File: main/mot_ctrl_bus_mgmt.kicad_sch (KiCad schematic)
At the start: 20 parts, among them Q1101 IRLML0030, U1101 74LS08

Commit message: Clean silkscreen
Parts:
- renumbered C1101 to C1601, D1101 to D1601, D1102 to D1602, D1103 to D1603, D1104 to D1604, D1105 to D1605, D1106 to D1606, JP1101 to JP1601, JP1102 to JP1602, JP1103 to JP1603, JP1104 to JP1604, Q1101 to Q1601, R1101 to R1601, R1102 to R1602, R1103 to R1603, R1104 to R1604, R1105 to R1605, R1106 to R1606, R1107 to R1607, U1101 to U1601

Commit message: Sent to fab
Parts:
- C1601: MPN (none) -> CL21B104KACNFNC; Mouser SKU (none) -> 187-CL21B104KACNFNC
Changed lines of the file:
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@@
+			)
+		)
+		(property "Quantity" ""
+			(at 231.14 48.26 0)
+			(effects
+				(font
+					(size 1.27 1.27)
+				)
 			)
 		)
@@
 			)
 		)
+		(property "Quantity" ""
+			(at 208.28 57.15 0)
+			(effects
+				(font
+					(size 1.27 1.27)
+				)
+			)
+		)
 		(pin "1"
 		)
@@
 			)
 		)
+		(property "Quantity" ""
+			(at 208.28 48.26 0)
+			(effects
+				(font
+					(size 1.27 1.27)
+				)
+			)
+		)
 		(pin "1"
 		)
@@
 			)
 		)
+		(property "Quantity" ""
+			(at 255.27 57.15 0)
+			(effects
+				(font
+					(size 1.27 1.27)
+				)
+			)
+		)
 		(pin "1"
 		)
@@
 				)
 				(hide yes)
+			)
+		)
+		(property "Quantity" ""
+			(at 219.71 57.15 0)
+			(effects
+				(font
+					(size 1.27 1.27)
+				)
 			)
 		)
@@
 			)
 		)
+		(property "Quantity" ""
+			(at 99.06 151.13 0)
+			(effects
+				(font
+					(size 1.27 1.27)
+				)
+			)
+		)
 		(pin "6"
 		)
@@
 			)
 		)
+		(property "Quantity" ""
+			(at 99.06 45.72 0)
+			(effects
+				(font
+					(size 1.27 1.27)
+				)
+			)
+		)
 		(pin "6"
 		)
@@
 			)
 		)
+		(property "Quantity" ""
+			(at 266.7 48.26 0)
+			(effects
+				(font
+					(size 1.27 1.27)
+				)
+			)
+		)
 		(pin "1"
 		)
@@
 			)
 		)
+		(property "MPN" "CL21B104KACNFNC "
+			(at 109.22 45.72 0)
+			(effects
+				(font
+					(size 1.27 1.27)
+				)
+			)
+		)
+		(property "Mouser SKU" " 187-CL21B104KACNFNC "
+			(at 109.22 45.72 0)
+			(effects
+				(font
+					(size 1.27 1.27)
+				)
+			)
+		)
+		(property "Quantity" ""
+			(at 109.22 45.72 0)
+			(effects
+				(font
+					(size 1.27 1.27)
+				)
+			)
+		)
 		(pin "1"
 		)
@@
 			)
 		)
+		(property "Quantity" ""
+			(at 99.06 100.33 0)
+			(effects
+				(font
+					(size 1.27 1.27)
+				)
+			)
+		)
 		(pin "6"
 		)
@@
 			)
 		)
+		(property "Quantity" ""
+			(at 109.22 93.98 0)
+			(effects
+				(font
+					(size 1.27 1.27)
+				)
+			)
+		)
 		(pin "2"
 		)
@@
 			)
 		)
+		(property "Quantity" ""
+			(at 250.19 81.28 0)
+			(effects
+				(font
+					(size 1.27 1.27)
+				)
+			)
+		)
 		(pin "2"
 		)
@@
 			)
 		)
+		(property "Quantity" ""
+			(at 243.84 57.15 0)
+			(effects
+				(font
+					(size 1.27 1.27)
+				)
+			)
+		)
 		(pin "1"
 		)
@@
 			)
 		)
+		(property "Quantity" ""
+			(at 109.22 119.38 0)
+			(effects
+				(font
+					(size 1.27 1.27)
+				)
+			)
+		)
 		(pin "2"
 		)
@@
 			)
 		)
+		(property "Quantity" ""
+			(at 109.22 144.78 0)
+			(effects
+				(font
+					(size 1.27 1.27)
+				)
+			)
+		)
 		(pin "2"
 		)
@@
 			)
 		)
+		(property "Quantity" ""
+			(at 99.06 26.67 0)
+			(effects
+				(font
+					(size 1.27 1.27)
+				)
+			)
+		)
 		(pin "2"
 		)
@@
 			)
 		)
+		(property "Quantity" ""
+			(at 231.14 57.15 0)
+			(effects
+				(font
+					(size 1.27 1.27)
+				)
+			)
+		)
 		(pin "1"
 		)
@@
 			)
 		)
+		(property "Quantity" ""
+			(at 266.7 57.15 0)
+			(effects
+				(font
+					(size 1.27 1.27)
+				)
+			)
+		)
 		(pin "1"
 		)
@@
 			)
 		)
+		(property "Quantity" ""
+			(at 99.06 171.45 0)
+			(effects
+				(font
+					(size 1.27 1.27)
+				)
+			)
+		)
 		(pin "6"
 		)
@@
 			)
 		)
+		(property "Quantity" ""
+			(at 255.27 48.26 0)
+			(effects
+				(font
+					(size 1.27 1.27)
+				)
+			)
+		)
 		(pin "1"
 		)
@@
 				)
 				(hide yes)
+			)
+		)
+		(property "Quantity" ""
+			(at 264.16 76.2 0)
+			(effects
+				(font
+					(size 1.27 1.27)
+				)
 			)
 		)
@@
 			)
 		)
+		(property "Quantity" ""
+			(at 99.06 125.73 0)
+			(effects
+				(font
+					(size 1.27 1.27)
+				)
+			)
+		)
 		(pin "6"
 		)
@@
 			)
 		)
+		(property "Quantity" ""
+			(at 243.84 48.26 0)
+			(effects
+				(font
+					(size 1.27 1.27)
+				)
+			)
+		)
 		(pin "1"
 		)
@@
 			)
 		)
+		(property "Quantity" ""
+			(at 219.71 48.26 0)
+			(effects
+				(font
+					(size 1.27 1.27)
+				)
+			)
+		)

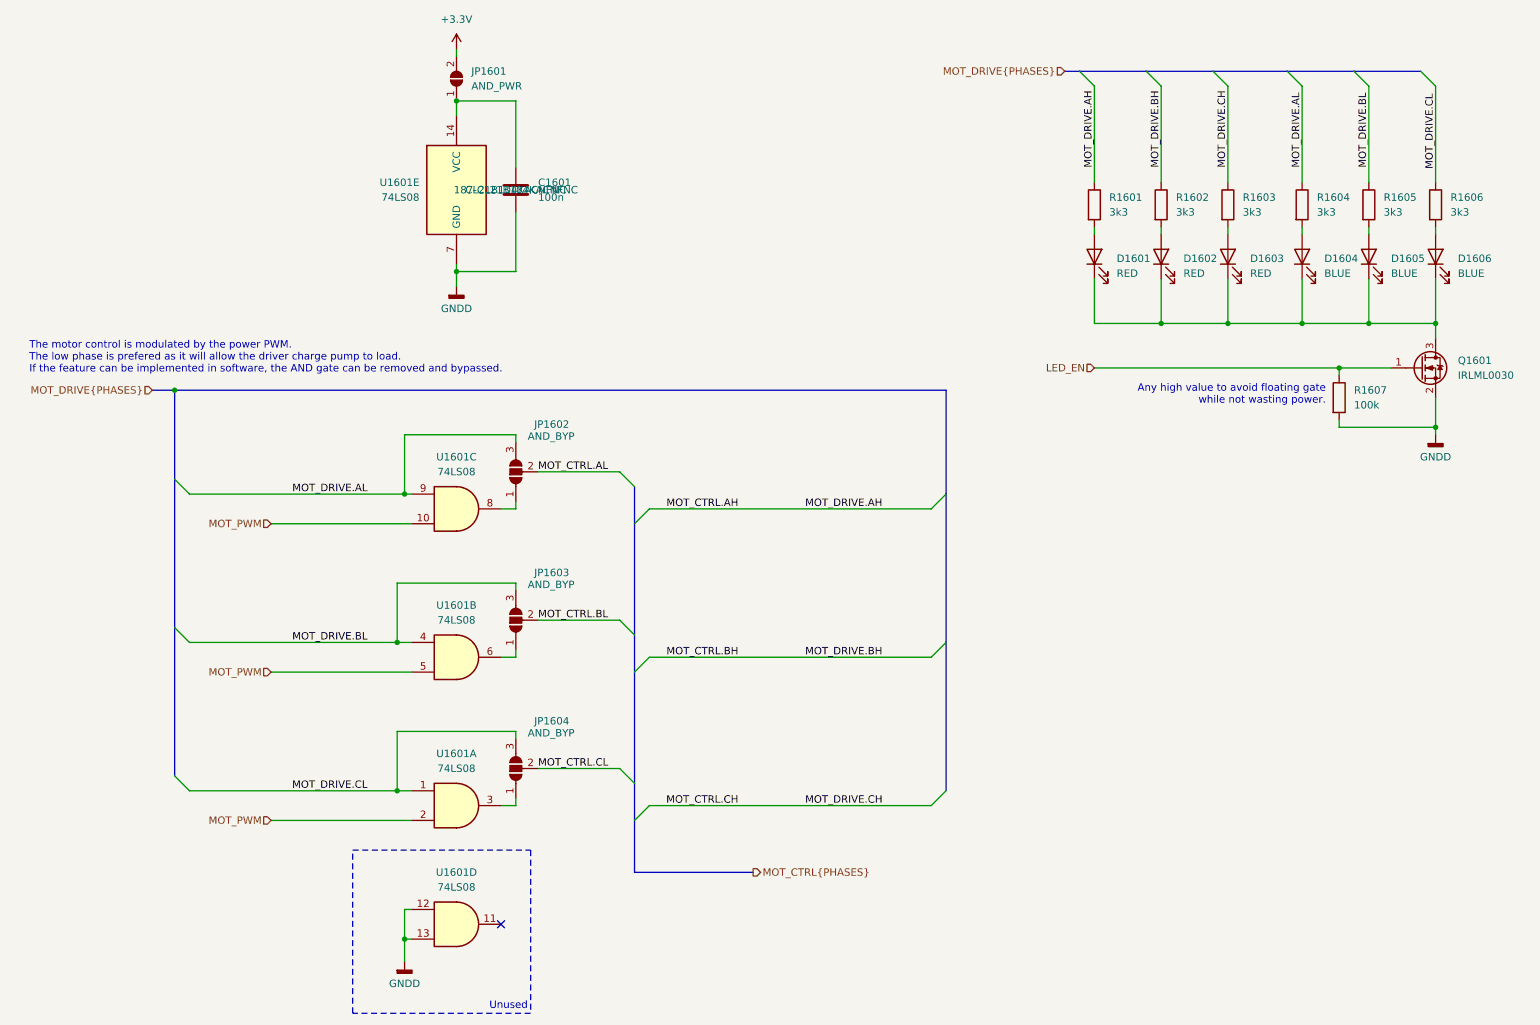
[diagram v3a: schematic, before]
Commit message: BOM almost OK, starts new side board.
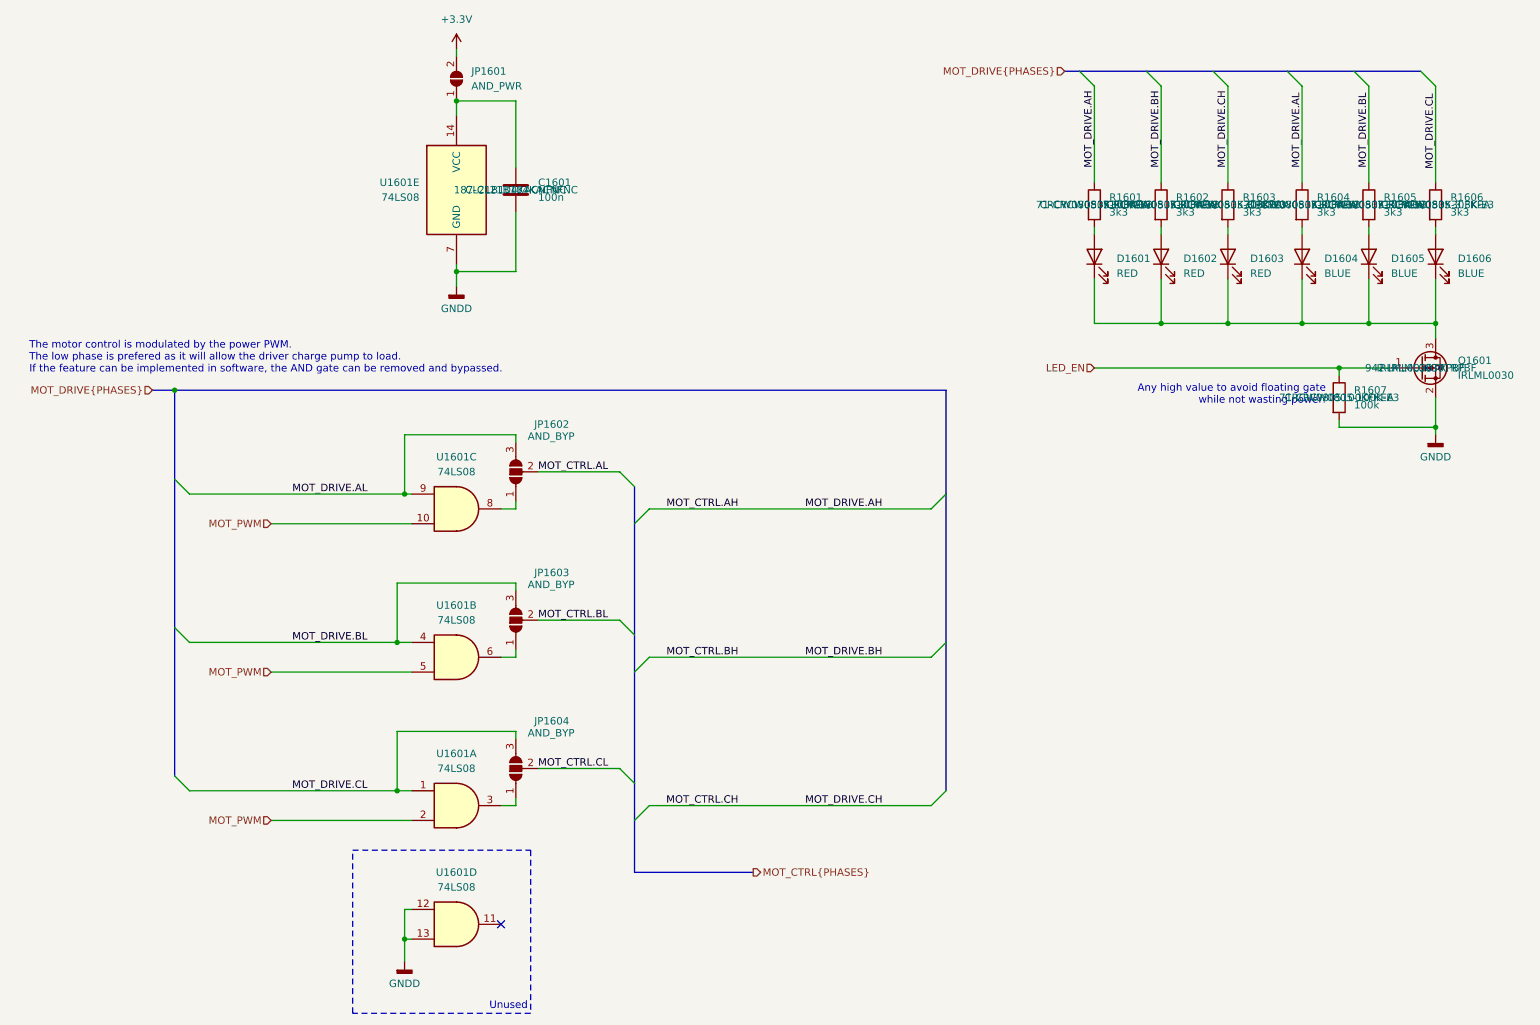
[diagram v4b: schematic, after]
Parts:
- JP1601, JP1602, JP1603, JP1604: now left out of the parts list
- Q1601: MPN (none) -> IRLML0030TRPBF; Mouser SKU (none) -> 942-IRLML0030TRPBF
- R1601, R1602, R1603, R1604, R1605, R1606: MPN (none) -> CRCW08053K30FKEA; Mouser SKU (none) -> 71-CRCW0805-3.3K-E3
- R1607: MPN (none) -> CRCW0805100KFKEA; Mouser SKU (none) -> 71-CRCW0805-100K-E3
- U1601: MPN 74LVC08ABQ,115 -> (none)
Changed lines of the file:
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@@
 (kicad_sch
-	(version 20240101)
+	(version 20240417)
 	(generator "eeschema")
 	(generator_version "8.99")
@@
 			)
 		)
+		(property "MPN" "CRCW08053K30FKEA"
+			(at 231.14 48.26 0)
+			(effects
+				(font
+					(size 1.27 1.27)
+				)
+			)
+		)
+		(property "Mouser SKU" " 71-CRCW0805-3.3K-E3 "
+			(at 231.14 48.26 0)
+			(effects
+				(font
+					(size 1.27 1.27)
+				)
+			)
+		)
 		(pin "1"
 		)
@@
 			)
 		)
+		(property "MPN" "CRCW08053K30FKEA"
+			(at 208.28 48.26 0)
+			(effects
+				(font
+					(size 1.27 1.27)
+				)
+			)
+		)
+		(property "Mouser SKU" " 71-CRCW0805-3.3K-E3 "
+			(at 208.28 48.26 0)
+			(effects
+				(font
+					(size 1.27 1.27)
+				)
+			)
+		)
 		(pin "1"
 		)
@@
 			)
 		)
-		(property "MPN" "74LVC08ABQ,115"
+		(property "MPN" ""
 			(at 99.06 151.13 0)
 			(effects
@@
 			)
 		)
-		(property "MPN" "74LVC08ABQ,115"
+		(property "MPN" ""
 			(at 99.06 45.72 0)
 			(effects
@@
 			)
 		)
+		(property "MPN" "CRCW08053K30FKEA"
+			(at 266.7 48.26 0)
+			(effects
+				(font
+					(size 1.27 1.27)
+				)
+			)
+		)
+		(property "Mouser SKU" " 71-CRCW0805-3.3K-E3 "
+			(at 266.7 48.26 0)
+			(effects
+				(font
+					(size 1.27 1.27)
+				)
+			)
+		)
 		(pin "1"
 		)
@@
 			)
 		)
-		(property "MPN" "74LVC08ABQ,115"
+		(property "MPN" ""
 			(at 99.06 100.33 0)
 			(effects
@@
 		(unit 1)
 		(exclude_from_sim no)
-		(in_bom yes)
+		(in_bom no)
 		(on_board yes)
 		(dnp no)
+		(fields_autoplaced yes)
 		(property "Reference" "JP1602"
 			(at 118.364 85.852 90)
@@
 			)
 		)
+		(property "MPN" "CRCW0805100KFKEA"
+			(at 250.19 81.28 0)
+			(effects
+				(font
+					(size 1.27 1.27)
+				)
+			)
+		)
+		(property "Mouser SKU" " 71-CRCW0805-100K-E3 "
+			(at 250.19 81.28 0)
+			(effects
+				(font
+					(size 1.27 1.27)
+				)
+			)
+		)
 		(pin "2"
 		)
@@
 		(unit 1)
 		(exclude_from_sim no)
-		(in_bom yes)
+		(in_bom no)
 		(on_board yes)
 		(dnp no)
+		(fields_autoplaced yes)
 		(property "Reference" "JP1603"
 			(at 118.364 111.252 90)
@@
 		(unit 1)
 		(exclude_from_sim no)
-		(in_bom yes)
+		(in_bom no)
 		(on_board yes)
 		(dnp no)
+		(fields_autoplaced yes)
 		(property "Reference" "JP1604"
 			(at 118.364 136.652 90)
@@
 		(unit 1)
 		(exclude_from_sim no)
-		(in_bom yes)
+		(in_bom no)
 		(on_board yes)
 		(dnp no)
@@
 			)
 		)
-		(property "MPN" "74LVC08ABQ,115"
+		(property "MPN" ""
 			(at 99.06 171.45 0)
 			(effects
@@
 			)
 		)
+		(property "MPN" "CRCW08053K30FKEA"
+			(at 255.27 48.26 0)
+			(effects
+				(font
+					(size 1.27 1.27)
+				)
+			)
+		)
+		(property "Mouser SKU" " 71-CRCW0805-3.3K-E3 "
+			(at 255.27 48.26 0)
+			(effects
+				(font
+					(size 1.27 1.27)
+				)
+			)
+		)
 		(pin "1"
 		)
@@
 		(on_board yes)
 		(dnp no)
-		(fields_autoplaced yes)
 		(property "Reference" "Q1601"
 			(at 270.51 74.9299 0)
@@
 			)
 		)
+		(property "MPN" "IRLML0030TRPBF"
+			(at 264.16 76.2 0)
+			(effects
+				(font
+					(size 1.27 1.27)
+				)
+			)
+		)
+		(property "Mouser SKU" "942-IRLML0030TRPBF "
+			(at 264.16 76.2 0)
+			(effects
+				(font
+					(size 1.27 1.27)
+				)
+			)
+		)
 		(pin "1"
 		)
@@
 			)
 		)
-		(property "MPN" "74LVC08ABQ,115"
+		(property "MPN" ""
 			(at 99.06 125.73 0)
 			(effects
@@
 			)
 		)
+		(property "MPN" "CRCW08053K30FKEA"
+			(at 243.84 48.26 0)
+			(effects
+				(font
+					(size 1.27 1.27)
+				)
+			)
+		)
+		(property "Mouser SKU" " 71-CRCW0805-3.3K-E3 "
+			(at 243.84 48.26 0)
+			(effects
+				(font
+					(size 1.27 1.27)
+				)
+			)
+		)
 		(pin "1"
 		)
@@
 			(at 219.71 48.26 0)
 			(effects
+				(font
+					(size 1.27 1.27)
+				)
+			)
+		)
+		(property "MPN" "CRCW08053K30FKEA"
+			(at 219.71 48.26 0)
+			(effects
+				(font
+					(size 1.27 1.27)
+				)
+			)
+		)
+		(property "Mouser SKU" " 71-CRCW0805-3.3K-E3 "
+			(at 219.71 48.26 0)
+			(effects

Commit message: Revised with BOM ordered
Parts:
- C1601: Mouser SKU 187-CL21B104KACNFNC -> 187-CL21B104KACNFNC
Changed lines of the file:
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@@
 			)
 		)
-		(property "Mouser SKU" " 187-CL21B104KACNFNC "
+		(property "Mouser SKU" "187-CL21B104KACNFNC "
 			(at 109.22 45.72 0)
 			(effects
